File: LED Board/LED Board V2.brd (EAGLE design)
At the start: 25.3 x 11.5 mm, 3 parts

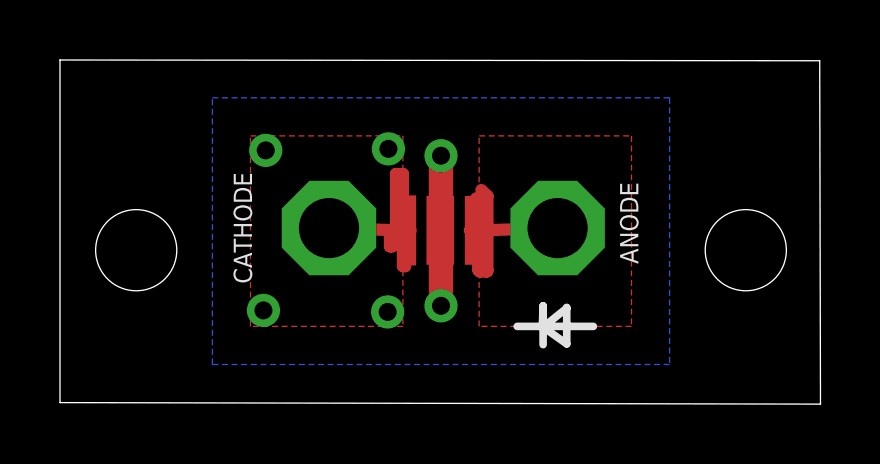
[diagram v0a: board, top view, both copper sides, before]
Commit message: Fixed dimensions of LED board
Also added measurement documentation on board.
Included png file of final board with measurements.
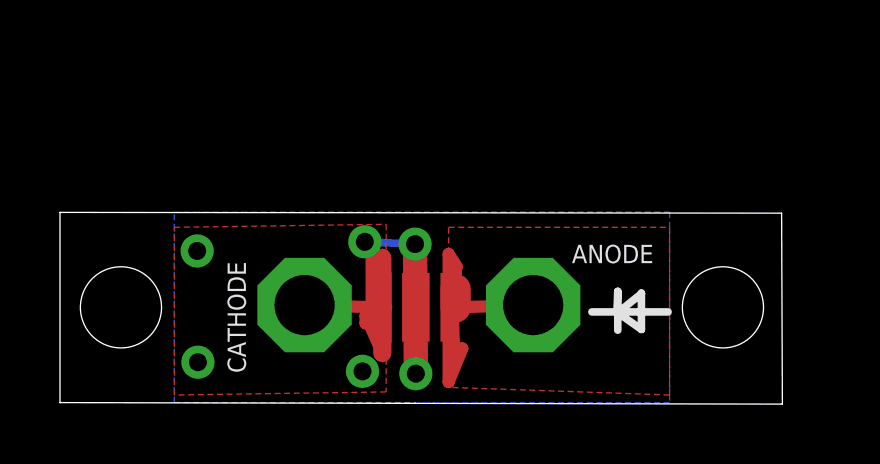
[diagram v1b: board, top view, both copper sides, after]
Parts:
- moved ANODE 2.69 mm to (15.8, 3.25)
- moved CATHODE 2.69 mm to (8.15, 3.25)
- moved D1 2.69 mm to (11.9, 3.17)
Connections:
- net CAM_LEDV renamed ANODE
- net GND renamed CATHODE
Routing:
- net ANODE: track 10.6 -> 14.3 mm
- net CATHODE: track 15.9 -> 19.3 mm, vias 2 -> 6
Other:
- board size 25.3 x 11.5 mm -> 24.1 x 6.4 mm
- board text added: "LENS OUTLINE 0.634 diameter"
- board text added: "all measurements in inches"
